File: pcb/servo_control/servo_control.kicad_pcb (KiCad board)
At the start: 2 copper layers, 94.6 x 62.9 mm, 50 parts, among them J1 Jack-DC, J10 Conn_01x03_Female, J11 Conn_01x03_Female, J12 Conn_01x03_Female, J13 Conn_01x03_Female, J14 Conn_01x03_Female, J15 Conn_01x03_Female, J16 Conn_01x03_Female, J17 Conn_01x03_Female, J18 Conn_01x03_Female, J19 Conn_01x03_Female, J2 YLIDAR X4, J20 Conn_01x03_Female, J21 Conn_01x06_Male, J22 GY-87, J3 Conn_01x03_Female, J4 Conn_01x03_Female, J5 Conn_01x03_Female, J6 Conn_01x03_Female, J7 Conn_01x03_Female, J8 Conn_01x03_Female, J9 Conn_01x03_Female, SW1 ESP_PROG, SW2 ESP_RST, U1 PCA9685BS, U2 LM317-3.3_SOT-223, U3 ESP32-WROOM-32, U4 MCP73213-A6SI/MF, U5 PCA9685BS, U6 LM317-5_SOT-223

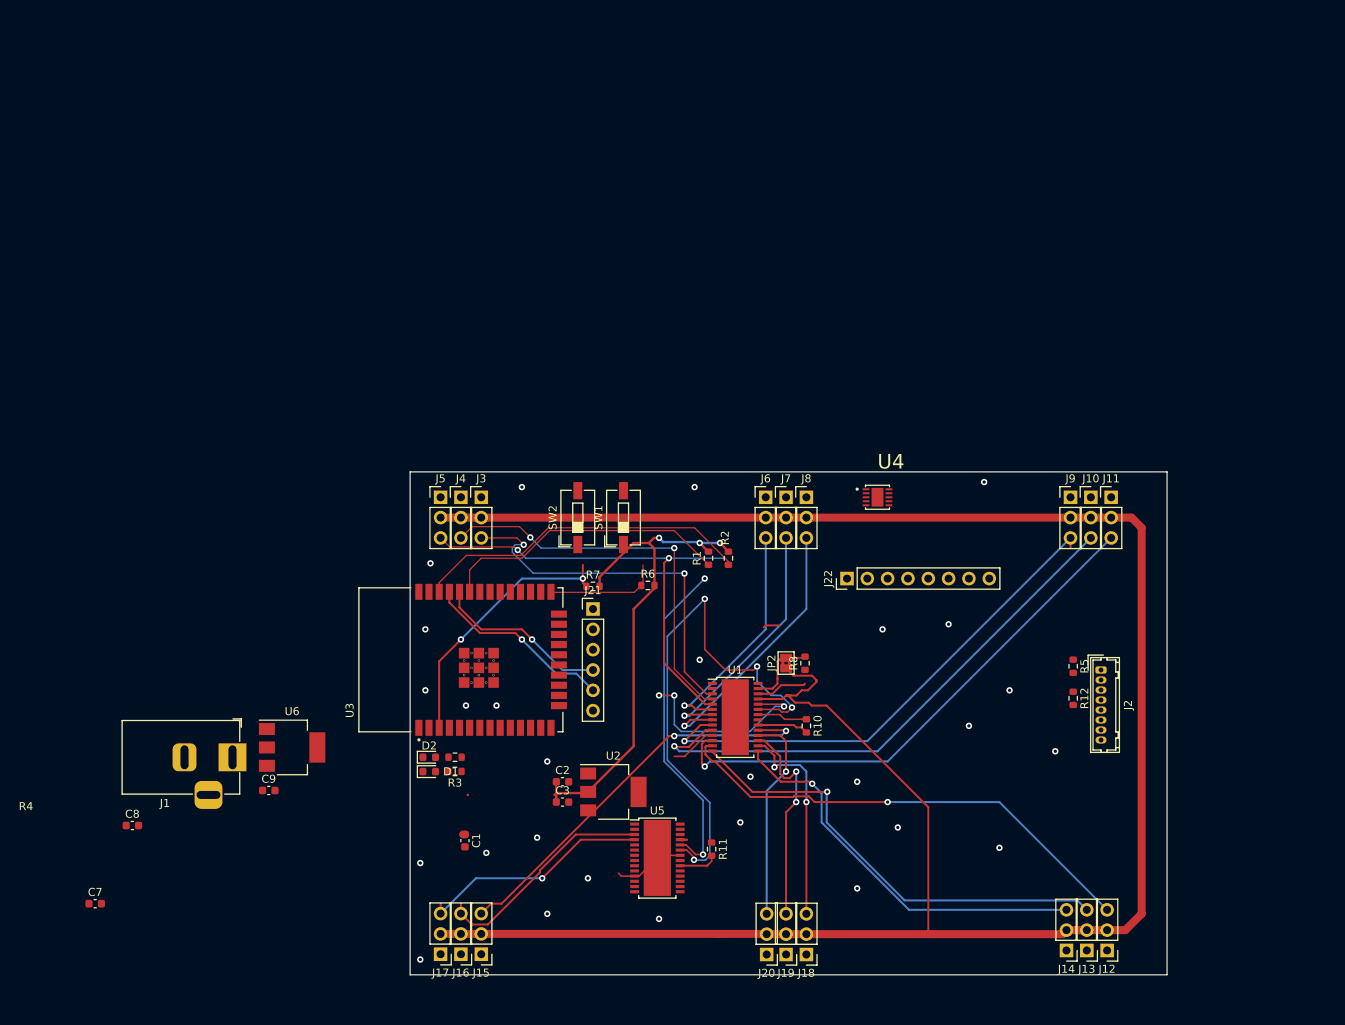
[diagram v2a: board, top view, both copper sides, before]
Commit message: add 18650 support + LT1085 regulator
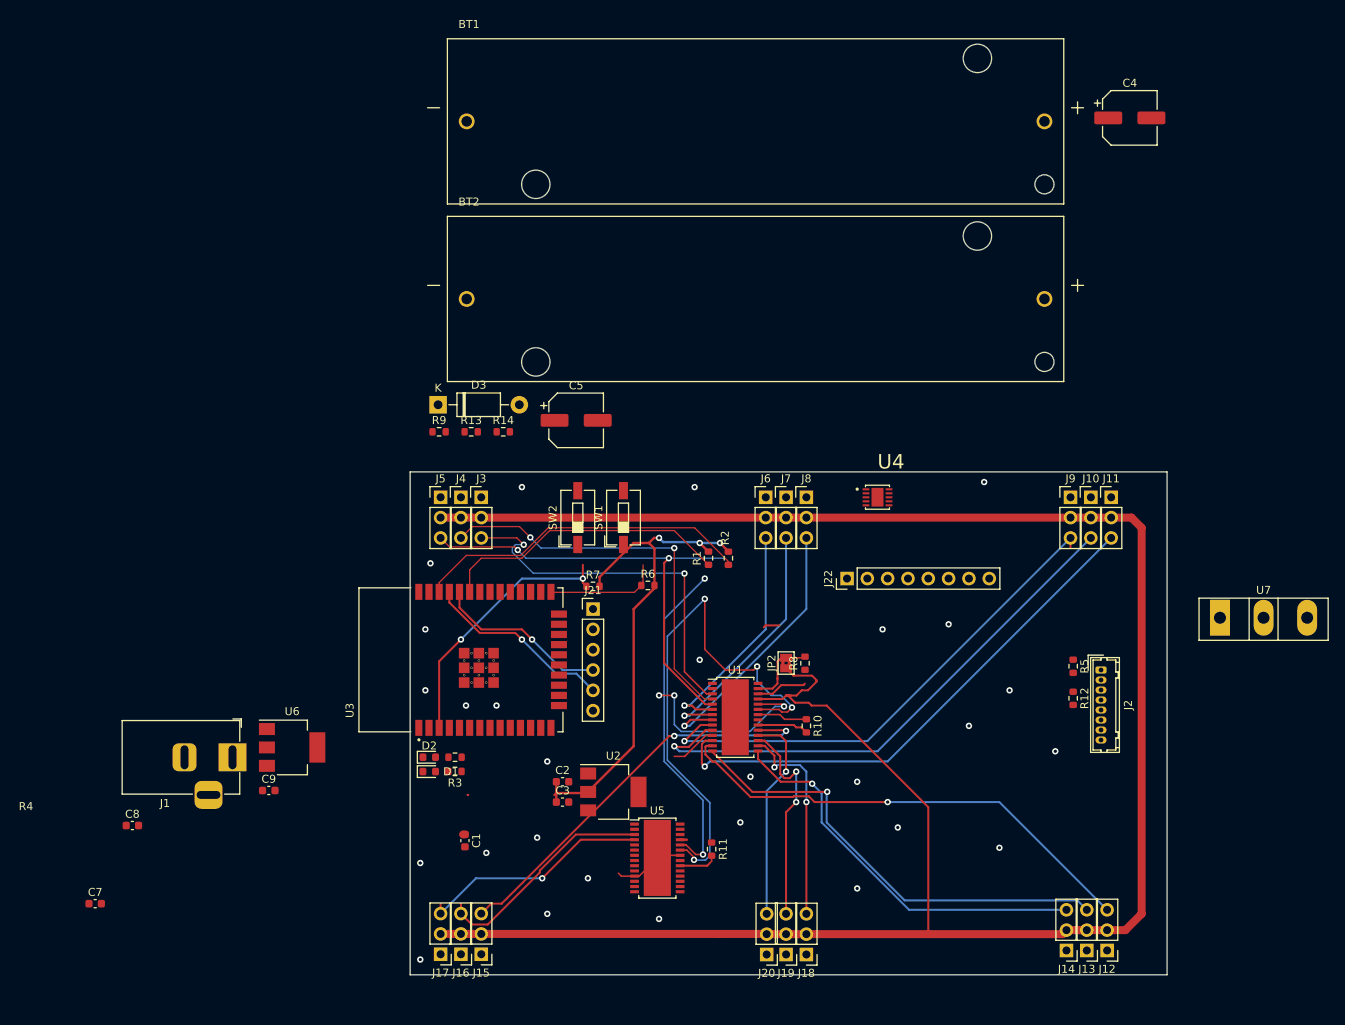
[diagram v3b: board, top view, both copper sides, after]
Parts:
- added BT1: 1043, 18650:BAT_1043, F.Cu at (143.5, -3.81)
- added BT2: 1043, 18650:BAT_1043, F.Cu at (143.5, 18.4)
- added C4: C_Polarized_US, Capacitor_SMD:CP_Elec_6.3x3, F.Cu at (190.3, -4.25)
- added C5: C_Polarized_US, Capacitor_SMD:CP_Elec_6.3x3, F.Cu at (121.1, 33.6)
- added D3: 1N4003, Diode_THT:D_DO-41_SOD81_P10.16mm_Horizontal, F.Cu at (103.8, 31.6)
- added R13: 240, Resistor_SMD:R_0603_1608Metric, F.Cu at (108.0, 35.0)
- added R14: 2K, Resistor_SMD:R_0603_1608Metric, F.Cu at (112.0, 35.0)
- added R9: 240, Resistor_SMD:R_0603_1608Metric, F.Cu at (104.0, 35.0)
- added U7: LT1085-ADJ, Package_TO_SOT_THT:TO-247-3_Vertical, F.Cu at (201.6, 58.2)
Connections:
- U4 pad 1: Net-(U4-Pad1) -> 9V
- U4 pad 10: unconnected-(U4-Pad10) -> Net-(U4-Pad10)
- U4 pad 2: Net-(U4-Pad1) -> 9V

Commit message: add 6V regulator
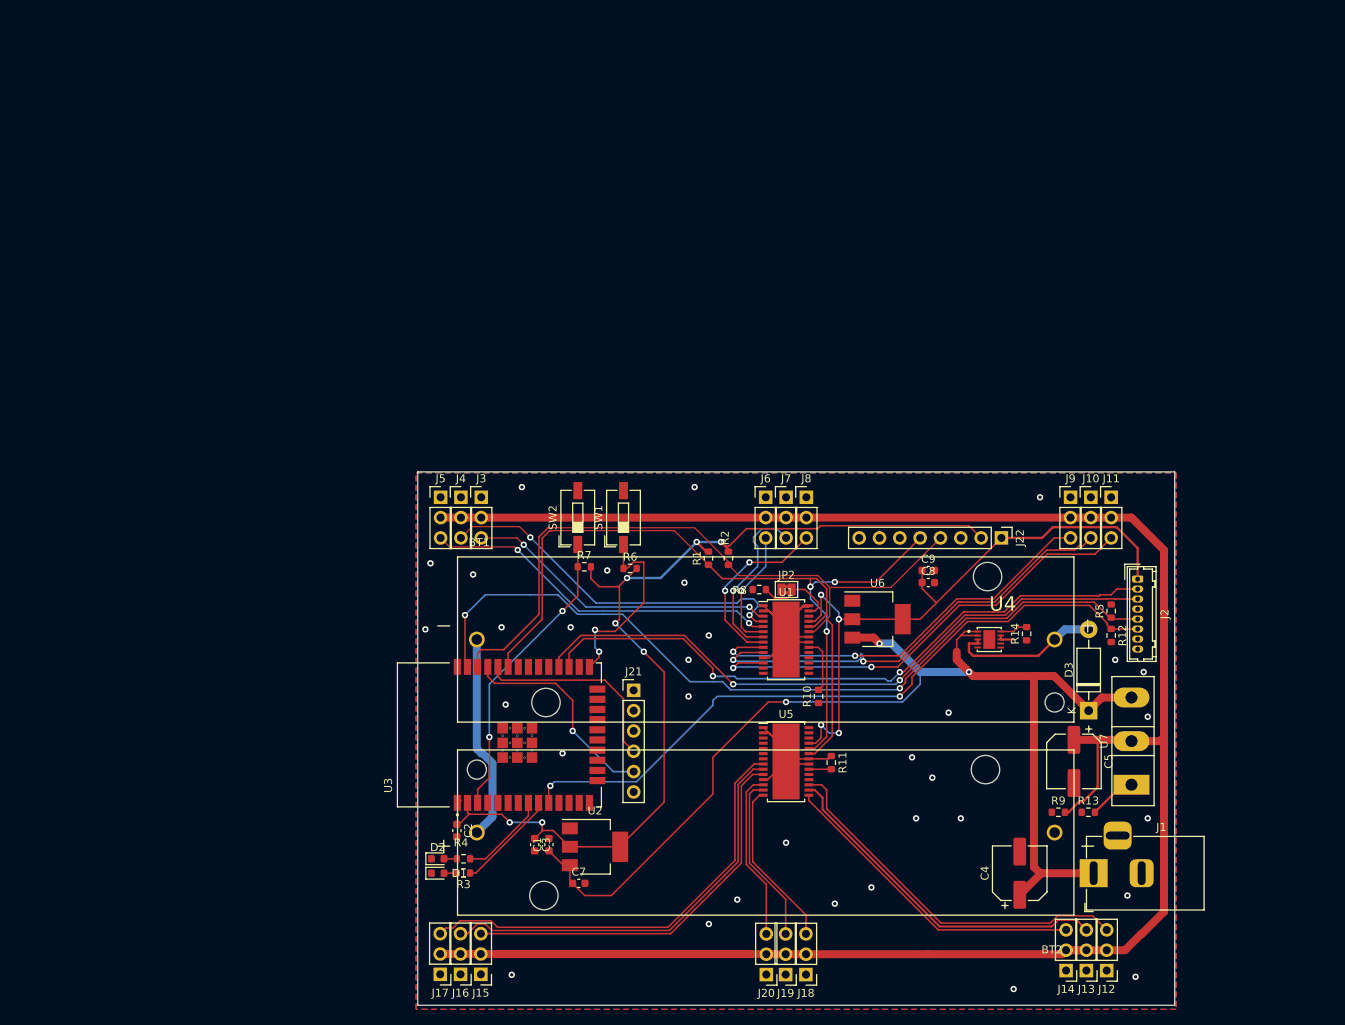
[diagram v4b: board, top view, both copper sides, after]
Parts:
- moved J1 108.6 mm to (185.8, 90.2), turned to 180 degrees
- moved C8 104.0 mm to (165.1, 53.8)
- moved C4 95.4 mm to (176.5, 90.2), turned to 90 degrees
- moved R9 90.8 mm to (181.4, 82.5)
- moved R13 90.6 mm to (185.1, 82.5)
- moved D3 89.9 mm to (185.2, 69.8), turned to 90 degrees
- moved C9 86.9 mm to (165.1, 52.3)
- moved C5 75.4 mm to (183.3, 76.2), turned to -90 degrees
- moved U6 74.9 mm to (158.8, 58.4)
- moved R14 70.1 mm to (177.4, 60.2), turned to 90 degrees
- moved BT2 66.7 mm to (144.8, 85.1), turned to 180 degrees
- moved BT1 64.8 mm to (144.8, 61.0)
- moved C7 60.5 mm to (121.4, 91.4)
- moved U7 23.6 mm to (190.5, 79.1), turned to 90 degrees
- moved U4 22.6 mm to (172.7, 61.0)
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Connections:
- J10 pad 2: VCC -> 6V
- J11 pad 2: VCC -> 6V
- J12 pad 2: VCC -> 6V
- J12 pad 3: PWM_0_9 -> PWM_1_13
- J13 pad 2: VCC -> 6V
- J13 pad 3: PWM_0_10 -> PWM_1_12
- J14 pad 2: VCC -> 6V
- J14 pad 3: PWM_0_11 -> PWM_1_11
- J15 pad 2: VCC -> 6V
- J15 pad 3: PWM_0_15 -> PWM_1_7
- J16 pad 2: VCC -> 6V
- J16 pad 3: PWM_1_0 -> PWM_1_6
- J17 pad 2: VCC -> 6V
- J17 pad 3: PWM_1_1 -> PWM_1_5
- J18 pad 2: VCC -> 6V
- J18 pad 3: PWM_0_12 -> PWM_1_10
- J19 pad 2: VCC -> 6V
- J19 pad 3: PWM_0_13 -> PWM_1_9
- J20 pad 2: VCC -> 6V
- J20 pad 3: PWM_0_14 -> PWM_1_8
- J3 pad 2: VCC -> 6V
- J4 pad 2: VCC -> 6V
- J5 pad 2: VCC -> 6V
- J6 pad 2: VCC -> 6V
- J7 pad 2: VCC -> 6V
- J8 pad 2: VCC -> 6V
- J9 pad 2: VCC -> 6V
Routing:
- net VCC: track 279.8 -> 0.00 mm
- net 6V: track 0.00 -> 254.2 mm
- net 9V: track 0.23 -> 149.7 mm, vias 0 -> 3
- net M_SCTR: track 0.00 -> 102.3 mm, vias 0 -> 2
- net DEV_EN: track 0.00 -> 87.2 mm, vias 0 -> 2
- net ESP_TX: track 0.00 -> 81.6 mm, vias 0 -> 2
- net ESP_RX: track 0.00 -> 81.0 mm, vias 0 -> 2
- net 5V: track 0.85 -> 80.5 mm, vias 0 -> 4
- net PWM_0_9: track 60.2 -> 0.00 mm, vias 1 -> 0
- net 3.3V: track 65.4 -> 123.1 mm, vias 3 -> 7
- net PWM_0_10: track 57.4 -> 0.00 mm, vias 1 -> 0
- net PWM_1_5: track 0.00 -> 55.5 mm
- net PWM_1_6: track 0.00 -> 52.7 mm
- net PWM_0_15: track 51.1 -> 0.00 mm, vias 2 -> 0
- net PWM_0_11: track 49.5 -> 0.00 mm, vias 1 -> 0
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- added copper zone on B.Cu, net GND
- added copper zone on F.Cu, net GND
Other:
- board size 94.6 x 62.9 mm -> 94.6 x 66.7 mm

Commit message: finish pcb
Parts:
- added D4: LED, LED_SMD:LED_0603_1608Metric, F.Cu at (180.3, 58.4)
- added R15: 10K, Resistor_SMD:R_0603_1608Metric, F.Cu at (188.0, 63.6)
- added R16: 1K, Resistor_SMD:R_0603_1608Metric, F.Cu at (183.2, 63.5)
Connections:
- JP2 pad 1: VCC -> 5V
- U3 pad 11: unconnected-(U3-Pad11) -> M_EN
- U4 pad 7: unconnected-(U4-Pad7) -> Net-(U4-Pad7)
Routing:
- net M_EN: track 0.00 -> 93.0 mm, vias 0 -> 2
- net Net-(U4-Pad7): track 0.00 -> 8.50 mm
- net 5V: track 80.5 -> 87.3 mm
- net Net-(D4-Pad2): track 0.00 -> 5.12 mm
- net 9V: track 149.7 -> 152.3 mm
- net I2C_SDA: track 102.9 -> 102.1 mm
- net Net-(R6-Pad1): track 23.9 -> 24.5 mm
- net ESP_TX: track 81.6 -> 82.2 mm
- net GND: vias 33 -> 39

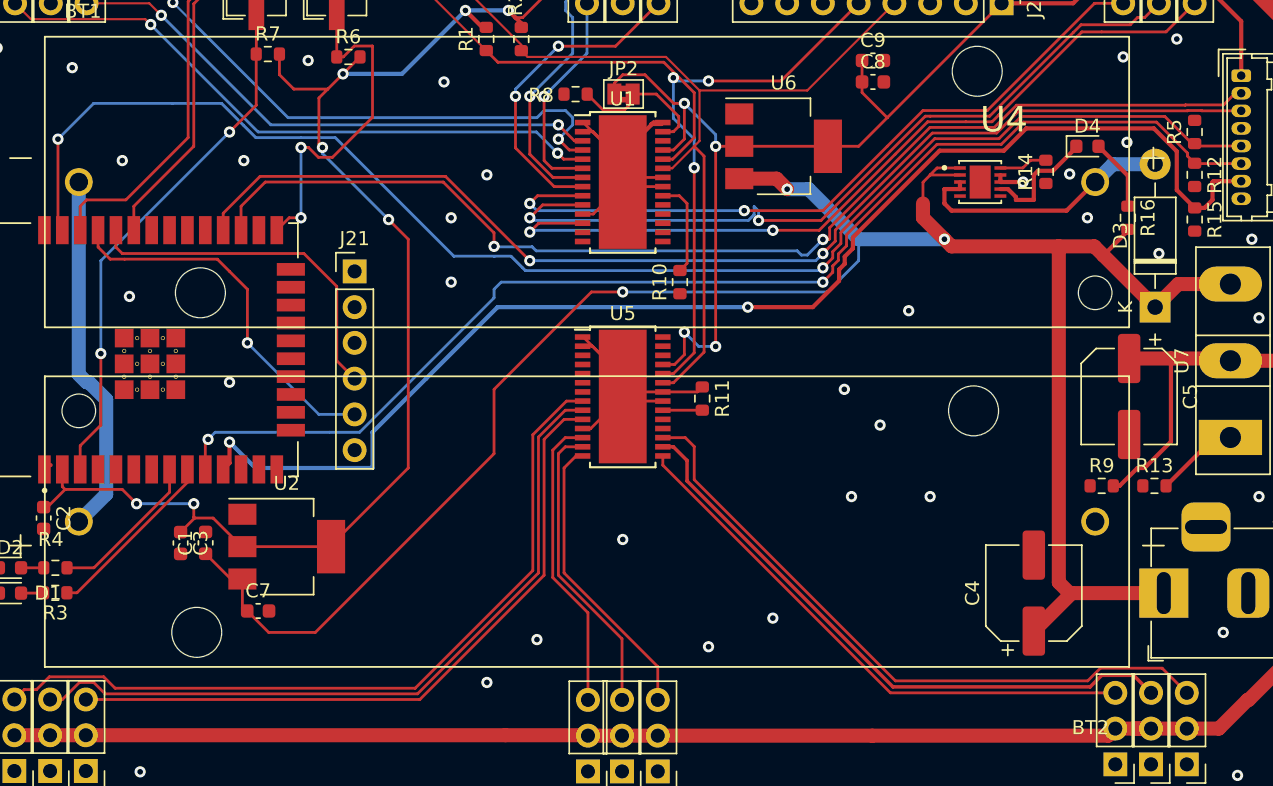
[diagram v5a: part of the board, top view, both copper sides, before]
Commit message: fix PCA9685 footprint
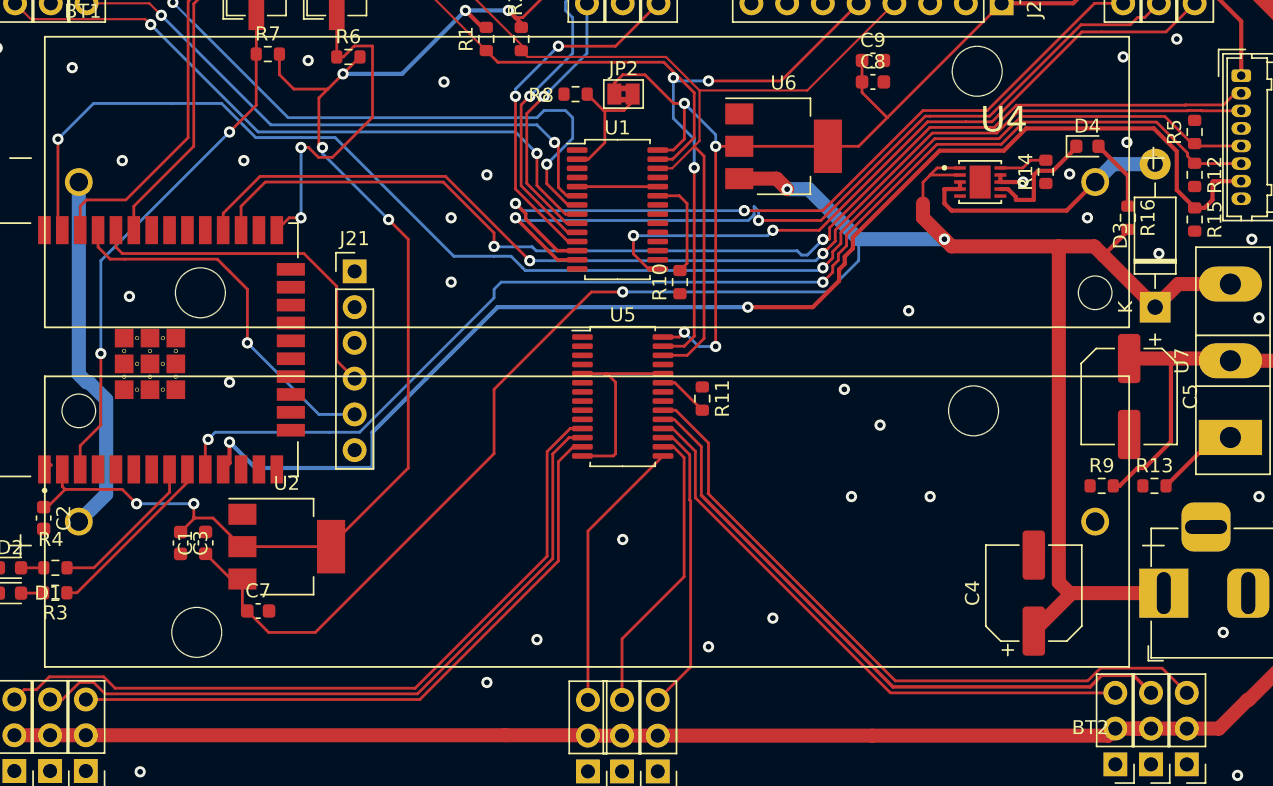
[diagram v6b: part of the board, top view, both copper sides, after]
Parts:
- U1, U5: value PCA9685BS -> PCA9685PW; footprint Package_SO:HTSSOP-28-1EP_4.4x9.7mm_P0.65mm_EP3.4x9.5mm -> Package_SO:TSSOP-28_4.4x9.7mm_P0.65mm
- moved U1 1.99 mm to (146.9, 62.9)
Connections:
- U1 pad 1: GND -> FIRST_A0
- U1 pad 10: PWM_0_7 -> PWM_0_4
- U1 pad 11: GND -> PWM_0_5
- U1 pad 12: PWM_0_8 -> PWM_0_6
- U1 pad 13: PWM_0_9 -> PWM_0_7
- U1 pad 14: PWM_0_10 -> GND
- U1 pad 15: PWM_0_11 -> PWM_0_8
- U1 pad 16: PWM_0_12 -> PWM_0_9
- U1 pad 17: PWM_0_13 -> PWM_0_10
- U1 pad 18: PWM_0_14 -> PWM_0_11
- U1 pad 19: PWM_0_15 -> PWM_0_12
- U1 pad 2: GND -> FIRST_A1
- U1 pad 20: Net-(R10-Pad2) -> PWM_0_13
- U1 pad 21: GND -> PWM_0_14
- U1 pad 22: GND -> PWM_0_15
- U1 pad 23: I2C_SCL -> Net-(R10-Pad2)
- U1 pad 24: I2C_SDA -> GND
- U1 pad 25: 5V -> GND
- U1 pad 26: FIRST_A0 -> I2C_SCL
- U1 pad 27: FIRST_A1 -> I2C_SDA
- U1 pad 28: GND -> 5V
- U1 pad 3: PWM_0_0 -> GND
- U1 pad 4: PWM_0_1 -> GND
- U1 pad 5: PWM_0_2 -> GND
- U1 pad 6: PWM_0_3 -> PWM_0_0
- U1 pad 7: PWM_0_4 -> PWM_0_1
- U1 pad 8: PWM_0_5 -> PWM_0_2
- U1 pad 9: PWM_0_6 -> PWM_0_3
- U5 pad 10: PWM_1_7 -> PWM_1_4
- U5 pad 11: GND -> PWM_1_5
- U5 pad 12: PWM_1_8 -> PWM_1_6
- U5 pad 13: PWM_1_9 -> PWM_1_7
- U5 pad 14: PWM_1_10 -> GND
- U5 pad 15: PWM_1_11 -> PWM_1_8
- U5 pad 16: PWM_1_12 -> PWM_1_9
- U5 pad 17: PWM_1_13 -> PWM_1_10
- U5 pad 18: PWM_1_14 -> PWM_1_11
- U5 pad 19: PWM_1_15 -> PWM_1_12
- U5 pad 20: Net-(R11-Pad2) -> PWM_1_13
- U5 pad 21: GND -> PWM_1_14
- U5 pad 22: GND -> PWM_1_15
- U5 pad 23: I2C_SCL -> Net-(R11-Pad2)
- U5 pad 24: I2C_SDA -> GND
- U5 pad 25: 5V -> GND
- U5 pad 26: GND -> I2C_SCL
- U5 pad 27: GND -> I2C_SDA
- U5 pad 28: GND -> 5V
- U5 pad 3: PWM_1_0 -> GND
- U5 pad 4: PWM_1_1 -> GND
- U5 pad 5: PWM_1_2 -> GND
- U5 pad 6: PWM_1_3 -> PWM_1_0
- U5 pad 7: PWM_1_4 -> PWM_1_1
- U5 pad 8: PWM_1_5 -> PWM_1_2
- U5 pad 9: PWM_1_6 -> PWM_1_3
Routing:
- net GND: track 51.5 -> 22.4 mm
- net PWM_0_8: track 58.0 -> 50.2 mm
- net PWM_0_1: track 46.0 -> 50.3 mm
- net PWM_0_3: track 15.4 -> 19.3 mm
- net PWM_0_4: track 21.7 -> 25.1 mm
- net PWM_0_6: track 52.5 -> 55.5 mm
- net PWM_0_5: track 22.8 -> 25.7 mm
- net PWM_0_2: track 44.9 -> 47.5 mm
- net PWM_0_0: track 39.3 -> 41.9 mm
- net PWM_0_7: track 56.9 -> 59.4 mm
- net PWM_1_11: track 39.5 -> 41.9 mm
- net PWM_1_7: track 49.2 -> 46.9 mm
- net PWM_1_6: track 52.7 -> 50.6 mm
- net PWM_1_5: track 55.5 -> 53.4 mm
- net PWM_1_12: track 43.5 -> 45.4 mm
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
